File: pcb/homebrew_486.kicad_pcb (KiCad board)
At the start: 4 copper layers, 150 x 150 mm, 162 parts, among them J1 Bus_ISA_16bit, J11 PEN, J13 KB, J15 PC SPK, J16 ATUART, J18 EXT. RESET, J19 Conn_01x02_Pin, J2 Bus_ISA_16bit, J20 Conn_01x02_Pin, J21 Conn_01x02_Pin, J22 Conn_01x02_Pin, J3 ATX-20, J4 AVR ISP, J5 Cmos settings, J6 Enable load, J9 x2 Multiplier, SW1 SW_SPDT, SW2 Reset, U1 486Socket, U10 8259A-2, U11 HM628512, U12 HM628512, U13 HM628512, U14 HM628512, U15 HM628512, U16 HM628512, U17 HM628512, U18 HM628512, U19 74LS245, U2 XC2S100TQ144, U20 74LS245, U21 W29C020, U22 ATmega128L-8A, U3 AMS1117, U4 AMS1117, U5 74LS245, U6 74LS245, U7 74LS245, U8 74LS245, U9 8254, Y1 TXC-7C, Y2 GTXO-14T, Y3 16MHz

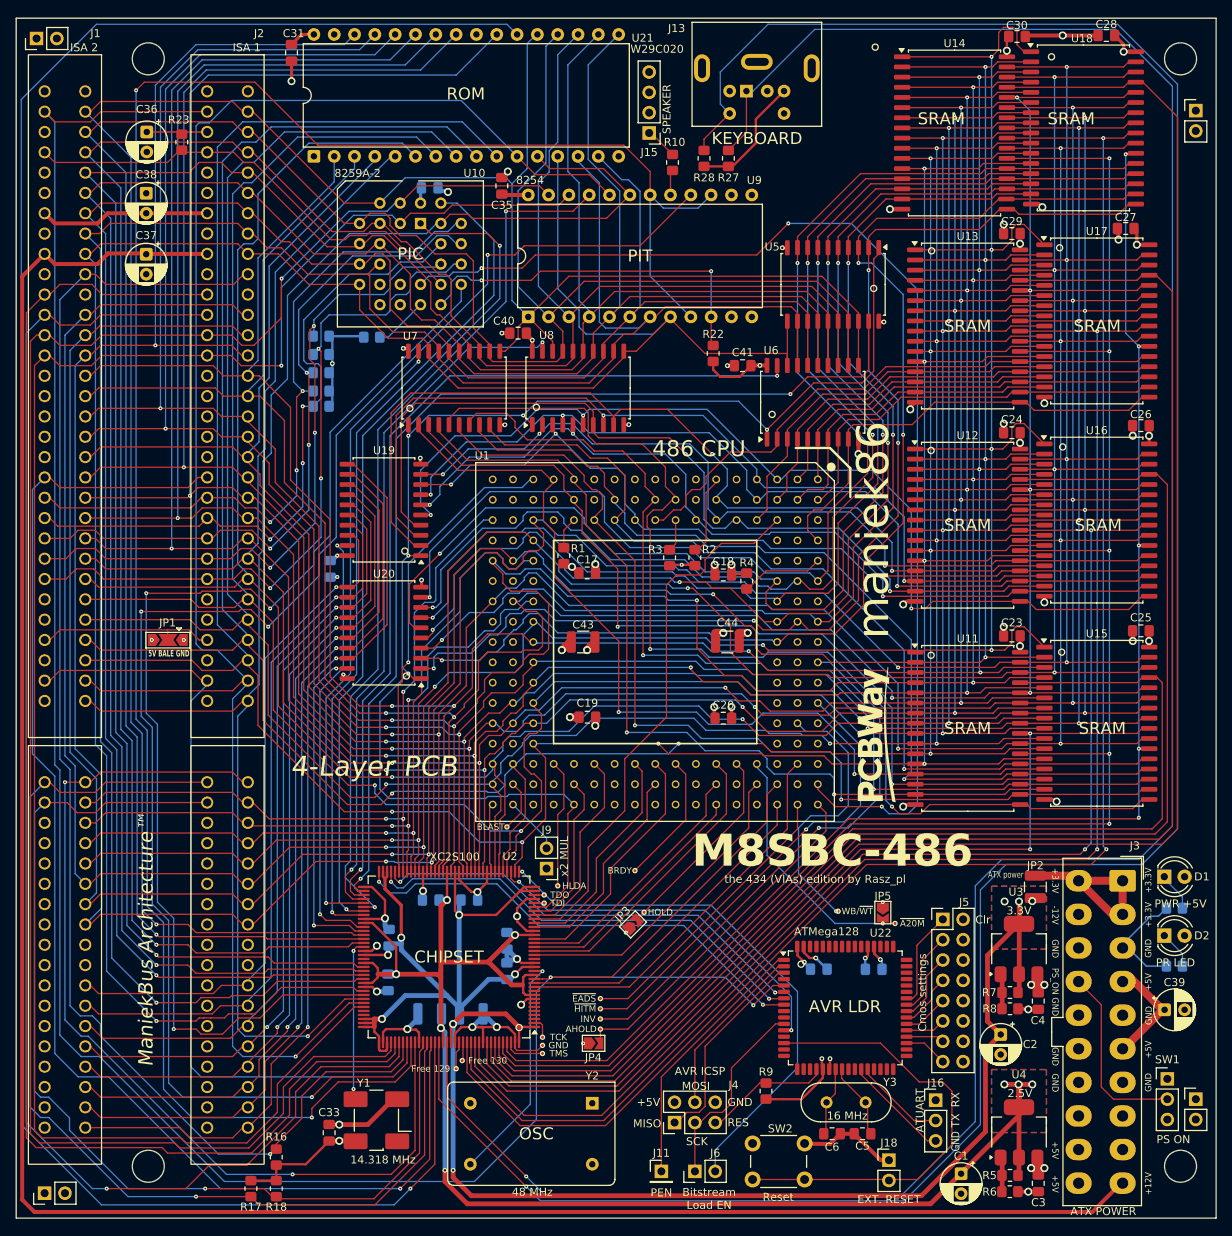
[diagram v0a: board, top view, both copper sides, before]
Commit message: PCB 425 VIAs
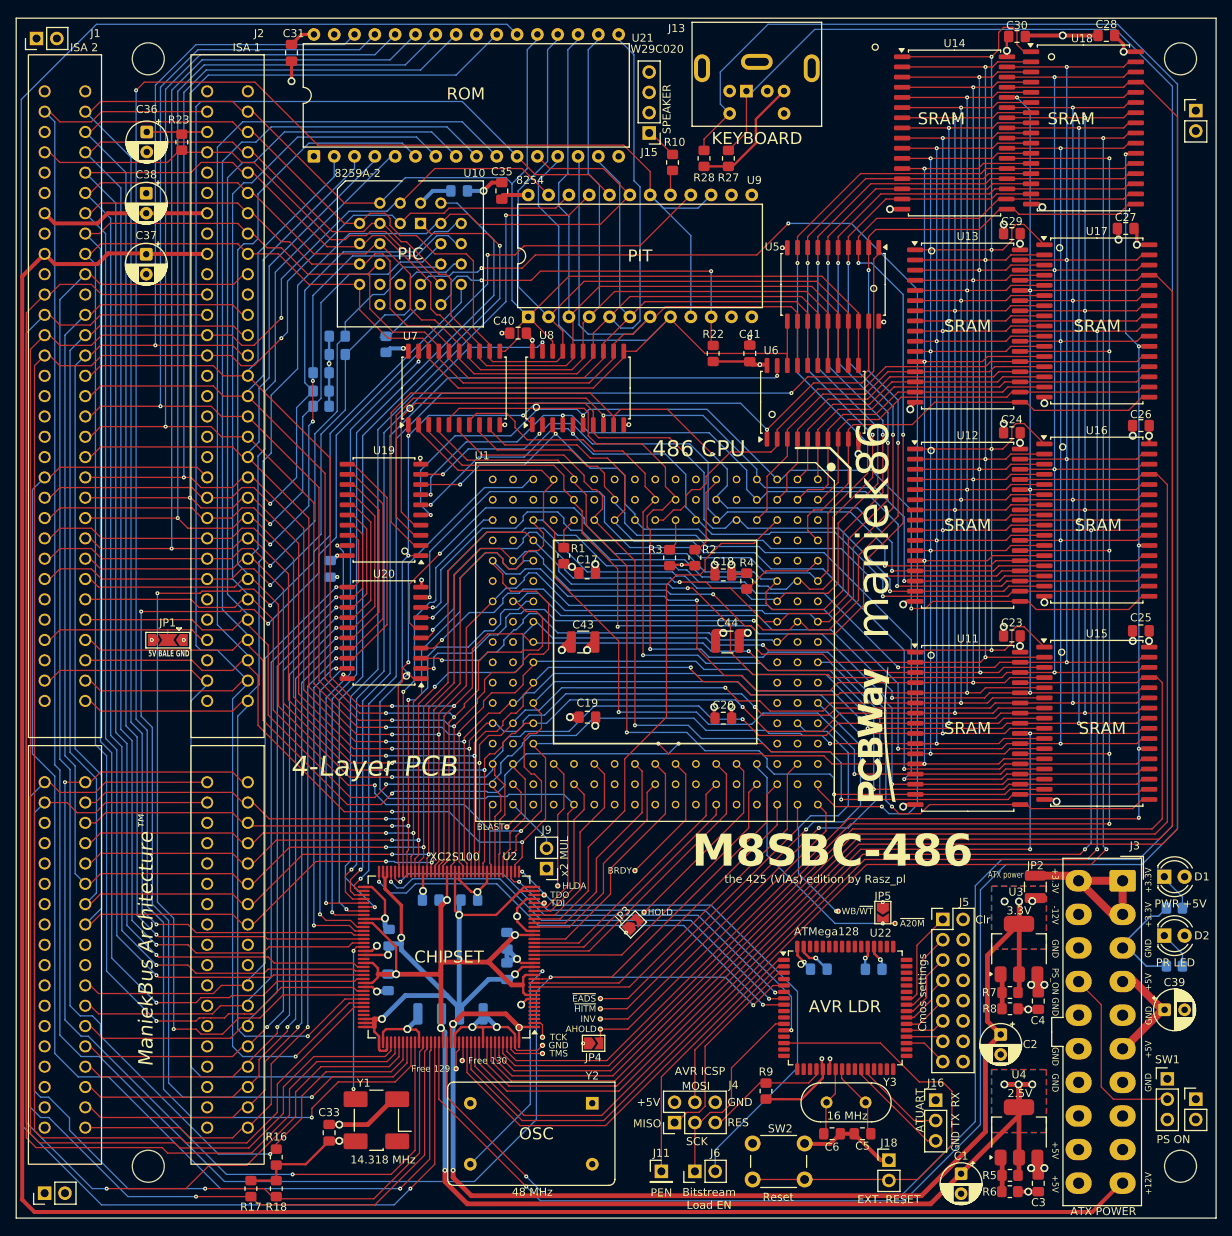
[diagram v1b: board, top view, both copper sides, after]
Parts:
- moved C32 3.70 mm to (77.0, 44.5)
- moved R24 2.02 mm to (61.7, 64.9), turned to 180 degrees
- moved R25 2.02 mm to (61.7, 62.6), turned to 180 degrees
- moved R26 1.99 mm to (67.8, 63.6), turned to -90 degrees
- moved C41 1.76 mm to (113.3, 64.8), turned to -90 degrees
- moved C35 0.64 mm to (82.3, 44.5)
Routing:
- net /ISA/IRQ3: track 90.0 -> 84.1 mm, vias 3 -> 1
- net /ISA/IRQ4: track 84.5 -> 79.4 mm, vias 3 -> 1
- net /ISA/IRQ6: track 82.1 -> 78.3 mm, vias 3 -> 1
- net /ISA/IRQ7: track 85.9 -> 82.3 mm, vias 3 -> 1
- net /DT0: track 271.9 -> 275.2 mm
- net /DT1: track 266.9 -> 269.7 mm
- net /ISA/IRQ5: track 86.9 -> 84.1 mm
- net /DT5: track 291.7 -> 289.0 mm
- net /KB_INT: track 149.1 -> 146.5 mm
- net /DT4: track 286.0 -> 283.6 mm
- net /DT2: track 263.9 -> 261.7 mm
- net /FPGA/~{IO_RD}: track 230.2 -> 228.2 mm
- net GND: track 166.3 -> 168.3 mm, vias 53 -> 52
- net /DT3: track 282.0 -> 284.0 mm
- net /SA11: track 150.2 -> 151.7 mm
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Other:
- board text added: "the 425 (VIAs) edition by Rasz_pl"
- board text removed: "the 434 (VIAs) edition by Rasz_pl"

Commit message: PCB 424 VIAs
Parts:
- moved R19 2.05 mm to (57.7, 69.3), turned to 0 degrees
- moved R20 2.05 mm to (57.7, 71.4), turned to 0 degrees
- moved R22 0.25 mm to (108.5, 64.8)
- moved R21 0.13 mm to (59.7, 67.1)
- moved R24 0.13 mm to (61.7, 64.8)
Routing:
- net +2V5: track 186.2 -> 193.0 mm
- net /PIT_SPK_GATE: track 197.9 -> 193.1 mm
- net /KB_INT: track 146.5 -> 143.7 mm
- net /ISA/IRQ6: track 78.3 -> 81.2 mm
- net +5V: track 141.2 -> 140.5 mm, vias 32 -> 33
- net /DT0: track 275.2 -> 274.6 mm
- net /DT15: track 113.9 -> 114.5 mm
- net /CPU/~{W/R}: track 174.6 -> 174.0 mm
- net /ISA/IRQ5: track 84.1 -> 83.5 mm, vias 3 -> 1
- net /DT14: track 109.0 -> 109.5 mm
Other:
- board text added: "the 424 (VIAs) edition by Rasz_pl"
- board text removed: "the 425 (VIAs) edition by Rasz_pl"
